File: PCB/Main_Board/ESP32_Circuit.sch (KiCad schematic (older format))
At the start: 26 parts, among them Q1 MBT3904DW1, SW2 EN, SW3 BOOT, U3 ESP32-WROOM-32, U4 FT231XS

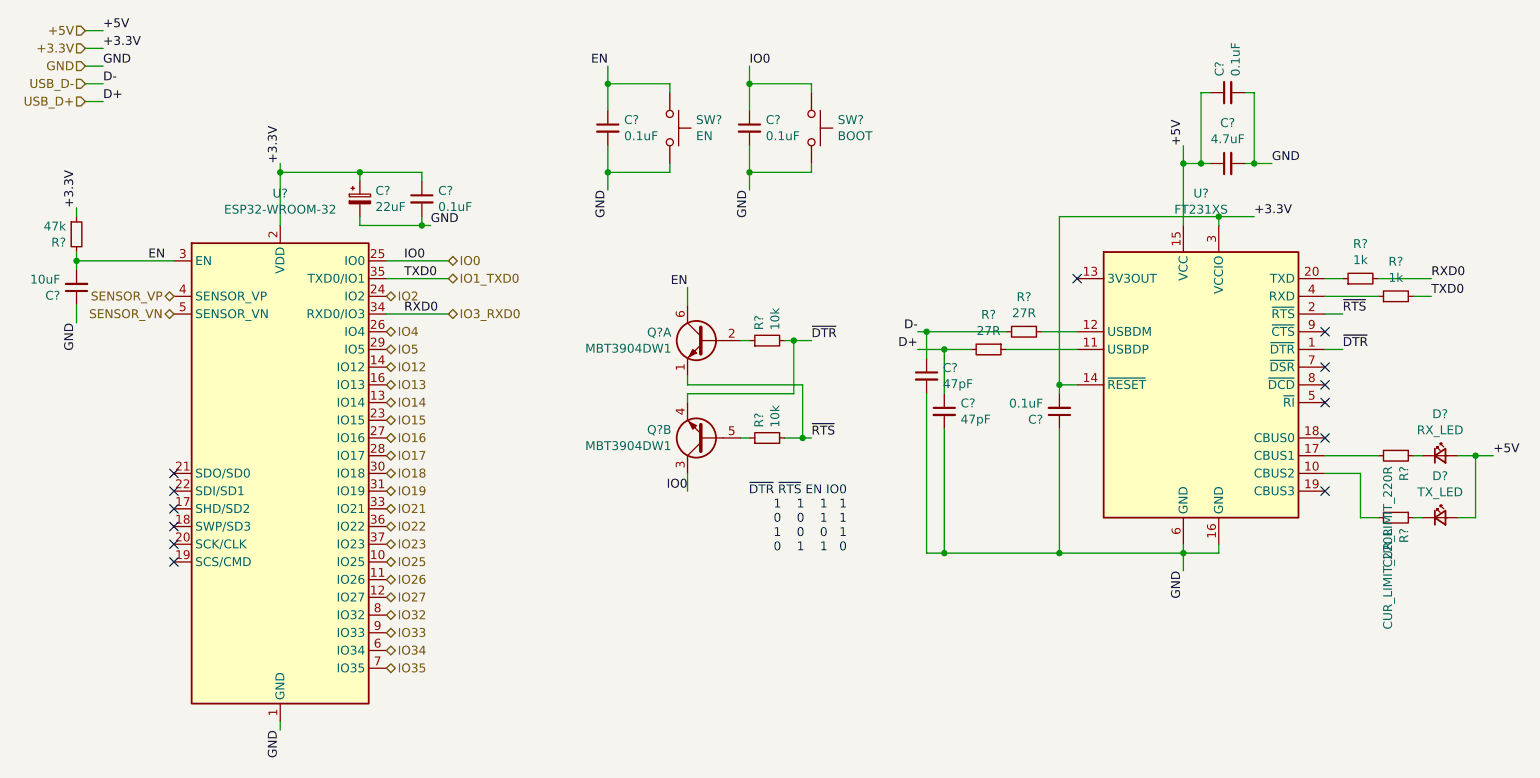
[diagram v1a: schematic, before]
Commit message: Annotate resistors
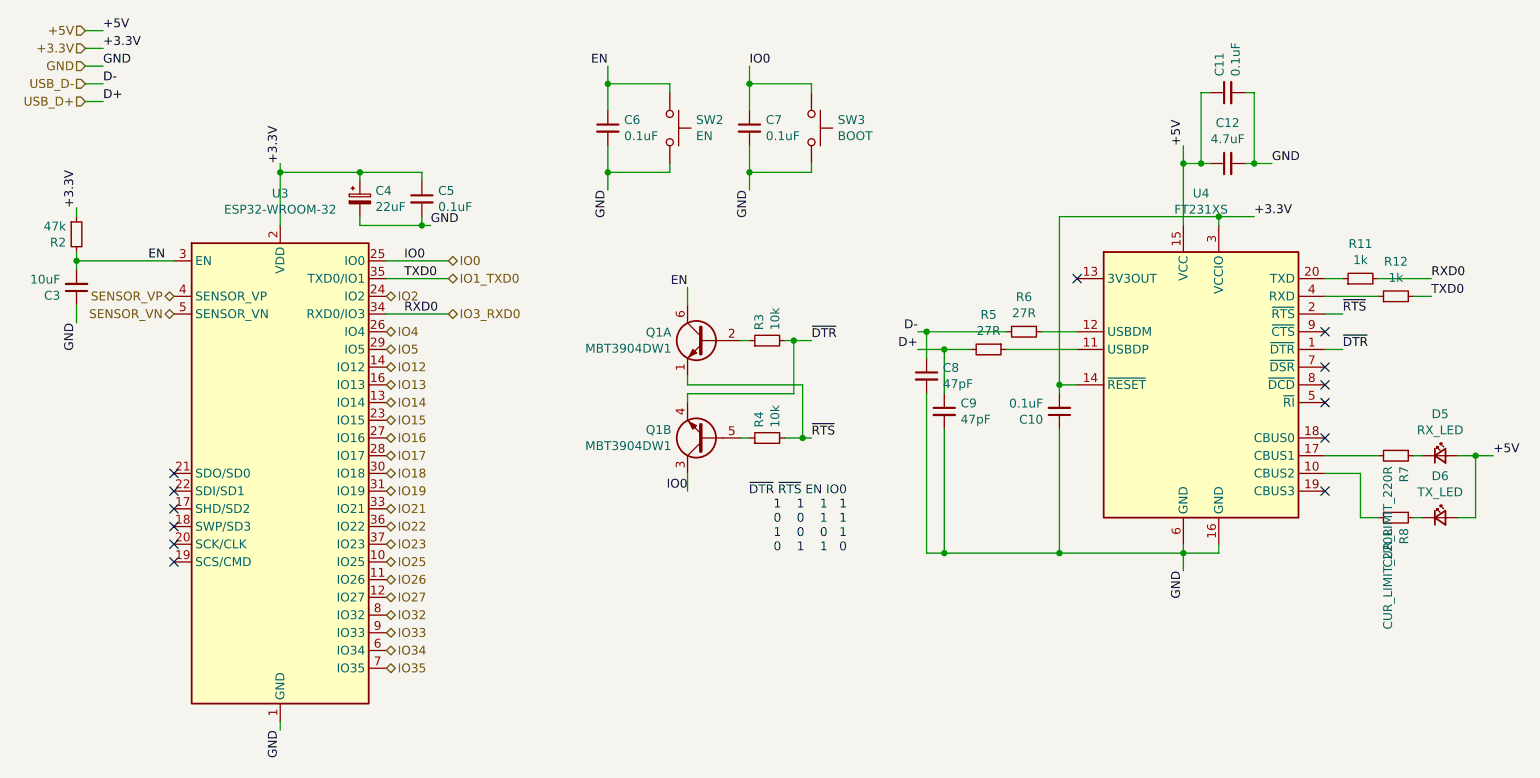
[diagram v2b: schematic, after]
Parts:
- gave numbers to parts that had none: 2
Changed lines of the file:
@@
 $Descr A4 11693 8268
 encoding utf-8
-Sheet 2 2
+Sheet 4 4
 Title "ESP32 Programming Circuit"
 Date "2020-09-10"
@@
 AR Path="/5F889015/5F5D6074" Ref="C12"  Part="1"
 AR Path="/5F80B999/5F5D6074" Ref="C?"  Part="1"
-F 0 "C?" V 8679 2400 50  0000 C CNN
+F 0 "C12" V 8679 2400 50  0000 C CNN
 F 1 "4.7uF" V 8588 2400 50  0000 C CNN
 F 2 "Capacitor_SMD:C_0603_1608Metric_Pad1.05x0.95mm_HandSolder" H 8450 2400 50  0001 C CNN
@@
 AR Path="/5F889015/5F5D607A" Ref="C11"  Part="1"
 AR Path="/5F80B999/5F5D607A" Ref="C?"  Part="1"
-F 0 "C?" H 8542 2046 50  0000 L CNN
+F 0 "C11" H 8542 2046 50  0000 L CNN
 F 1 "0.1uF" H 8542 1955 50  0000 L CNN
 F 2 "Capacitor_SMD:C_0603_1608Metric_Pad1.05x0.95mm_HandSolder" H 8450 2000 50  0001 C CNN
@@
 AR Path="/5F889015/5F5D6093" Ref="C10"  Part="1"
 AR Path="/5F80B999/5F5D6093" Ref="C?"  Part="1"
-F 0 "C?" H 7592 3846 50  0000 L CNN
+F 0 "C10" H 7592 3846 50  0000 L CNN
 F 1 "0.1uF" H 7592 3755 50  0000 L CNN
 F 2 "Capacitor_SMD:C_0603_1608Metric_Pad1.05x0.95mm_HandSolder" H 7500 3800 50  0001 C CNN
@@
 AR Path="/5F889015/5F5D60AB" Ref="C8"  Part="1"
 AR Path="/5F80B999/5F5D60AB" Ref="C?"  Part="1"
-F 0 "C?" H 6842 3646 50  0000 L CNN
+F 0 "C8" H 6842 3646 50  0000 L CNN
 F 1 "47pF" H 6842 3555 50  0000 L CNN
 F 2 "Capacitor_SMD:C_0603_1608Metric_Pad1.05x0.95mm_HandSolder" H 6750 3600 50  0001 C CNN
@@
 AR Path="/5F889015/5F5D60B1" Ref="C9"  Part="1"
 AR Path="/5F80B999/5F5D60B1" Ref="C?"  Part="1"
-F 0 "C?" H 6942 3846 50  0000 L CNN
+F 0 "C9" H 6942 3846 50  0000 L CNN
 F 1 "47pF" H 6942 3755 50  0000 L CNN
 F 2 "Capacitor_SMD:C_0603_1608Metric_Pad1.05x0.95mm_HandSolder" H 6850 3800 50  0001 C CNN
@@
 AR Path="/5F889015/5F5D60CE" Ref="U4"  Part="1"
 AR Path="/5F80B999/5F5D60CE" Ref="U?"  Part="1"
-F 0 "U?" H 8300 4731 50  0000 C CNN
+F 0 "U4" H 8300 4731 50  0000 C CNN
 F 1 "FT231XS" H 8300 4640 50  0000 C CNN
 F 2 "Package_SO:SSOP-20_3.9x8.7mm_P0.635mm" H 9300 2850 50  0001 C CNN
@@
 AR Path="/5F889015/5F5D60D4" Ref="D6"  Part="1"
 AR Path="/5F80B999/5F5D60D4" Ref="D?"  Part="1"
-F 0 "D?" H 9650 4635 50  0000 C CNN
+F 0 "D6" H 9650 4635 50  0000 C CNN
 F 1 "TX_LED" H 9650 4544 50  0000 C CNN
 F 2 "LED_SMD:LED_0603_1608Metric_Pad1.05x0.95mm_HandSolder" V 9650 4400 50  0001 C CNN
@@
 AR Path="/5F889015/5F5D60DB" Ref="R8"  Part="1"
 AR Path="/5F80B999/5F5D60DB" Ref="R?"  Part="1"
-F 0 "R?" H 9459 4446 50  0000 L CNN
+F 0 "R8" H 9459 4446 50  0000 L CNN
 F 1 "CUR_LIMIT_220R" H 9459 4355 50  0000 L CNN
 F 2 "Resistor_SMD:R_0603_1608Metric_Pad1.05x0.95mm_HandSolder" H 9400 4400 50  0001 C CNN
@@
 AR Path="/5F889015/5F5D60E1" Ref="D5"  Part="1"
 AR Path="/5F80B999/5F5D60E1" Ref="D?"  Part="1"
-F 0 "D?" H 9650 4285 50  0000 C CNN
+F 0 "D5" H 9650 4285 50  0000 C CNN
 F 1 "RX_LED" H 9650 4194 50  0000 C CNN
 F 2 "LED_SMD:LED_0603_1608Metric_Pad1.05x0.95mm_HandSolder" V 9650 4050 50  0001 C CNN
@@
 AR Path="/5F889015/5F5D60E8" Ref="R7"  Part="1"
 AR Path="/5F80B999/5F5D60E8" Ref="R?"  Part="1"
-F 0 "R?" H 9459 4096 50  0000 L CNN
+F 0 "R7" H 9459 4096 50  0000 L CNN
 F 1 "CUR_LIMIT_220R" H 9459 4005 50  0000 L CNN
 F 2 "Resistor_SMD:R_0603_1608Metric_Pad1.05x0.95mm_HandSolder" H 9400 4050 50  0001 C CNN
@@
 AR Path="/5F889015/5F5F2511" Ref="U3"  Part="1"
 AR Path="/5F80B999/5F5F2511" Ref="U?"  Part="1"
-F 0 "U?" H 3100 5731 50  0000 C CNN
+F 0 "U3" H 3100 5731 50  0000 C CNN
 F 1 "ESP32-WROOM-32" H 3100 5640 50  0000 C CNN
 F 2 "RF_Module:ESP32-WROOM-32" H 3100 2650 50  0001 C CNN
@@
 AR Path="/5F889015/5F5F251D" Ref="C4"  Part="1"
 AR Path="/5F80B999/5F5F251D" Ref="C?"  Part="1"
-F 0 "C?" H 3638 2646 50  0000 L CNN
+F 0 "C4" H 3638 2646 50  0000 L CNN
 F 1 "22uF" H 3638 2555 50  0000 L CNN
 F 2 "Capacitor_SMD:C_0603_1608Metric_Pad1.05x0.95mm_HandSolder" H 3550 2600 50  0001 C CNN
@@
 AR Path="/5F889015/5F5F2523" Ref="C5"  Part="1"
 AR Path="/5F80B999/5F5F2523" Ref="C?"  Part="1"
-F 0 "C?" H 3992 2646 50  0000 L CNN
+F 0 "C5" H 3992 2646 50  0000 L CNN
 F 1 "0.1uF" H 3992 2555 50  0000 L CNN
 F 2 "Capacitor_SMD:C_0603_1608Metric_Pad1.05x0.95mm_HandSolder" H 3900 2600 50  0001 C CNN
@@
 AR Path="/5F889015/5F5F2548" Ref="C3"  Part="1"
 AR Path="/5F80B999/5F5F2548" Ref="C?"  Part="1"
-F 0 "C?" H 2042 3146 50  0000 L CNN
+F 0 "C3" H 2042 3146 50  0000 L CNN
 F 1 "10uF" H 2042 3055 50  0000 L CNN
 F 2 "Capacitor_SMD:C_0603_1608Metric_Pad1.05x0.95mm_HandSolder" H 1950 3100 50  0001 C CNN
@@
 AR Path="/5F889015/5F5F254F" Ref="C6"  Part="1"
 AR Path="/5F80B999/5F5F254F" Ref="C?"  Part="1"
-F 0 "C?" H 5042 2246 50  0000 L CNN
+F 0 "C6" H 5042 2246 50  0000 L CNN
 F 1 "0.1uF" H 5042 2155 50  0000 L CNN
 F 2 "Capacitor_SMD:C_0603_1608Metric_Pad1.05x0.95mm_HandSolder" H 4950 2200 50  0001 C CNN
@@
 AR Path="/5F889015/5F5F2568" Ref="SW2"  Part="1"
 AR Path="/5F80B999/5F5F2568" Ref="SW?"  Part="1"
-F 0 "SW?" V 5254 2348 50  0000 L CNN
+F 0 "SW2" V 5254 2348 50  0000 L CNN
 F 1 "EN" V 5345 2348 50  0000 L CNN
 F 2 "SamacSys:SKTHAHE010" H 5300 2400 50  0001 C CNN
@@
 AR Path="/5F889015/5F5F2577" Ref="C7"  Part="1"
 AR Path="/5F80B999/5F5F2577" Ref="C?"  Part="1"
-F 0 "C?" H 5842 2246 50  0000 L CNN
+F 0 "C7" H 5842 2246 50  0000 L CNN
 F 1 "0.1uF" H 5842 2155 50  0000 L CNN
 F 2 "Capacitor_SMD:C_0603_1608Metric_Pad1.05x0.95mm_HandSolder" H 5750 2200 50  0001 C CNN
@@
 AR Path="/5F889015/5F5F258F" Ref="SW3"  Part="1"
 AR Path="/5F80B999/5F5F258F" Ref="SW?"  Part="1"
-F 0 "SW?" V 6054 2348 50  0000 L CNN
+F 0 "SW3" V 6054 2348 50  0000 L CNN
 F 1 "BOOT" V 6145 2348 50  0000 L CNN
 F 2 "SamacSys:SKTHAHE010" H 6100 2400 50  0001 C CNN
@@
 AR Path="/5F889015/5F5F2599" Ref="Q1"  Part="1"
 AR Path="/5F80B999/5F5F2599" Ref="Q?"  Part="1"
-F 0 "Q?" H 5691 3446 50  0000 L CNN
+F 0 "Q1" H 5691 3446 50  0000 L CNN
 F 1 "MBT3904DW1" H 5691 3355 50  0000 L CNN
 F 2 "Package_TO_SOT_SMD:SOT-363_SC-70-6" H 5700 3500 50  0001 C CNN
@@
 AR Path="/5F889015/5F5F259F" Ref="Q1"  Part="2"
 AR Path="/5F80B999/5F5F259F" Ref="Q?"  Part="2"
-F 0 "Q?" H 5691 3904 50  0000 L CNN
+F 0 "Q1" H 5691 3904 50  0000 L CNN
 F 1 "MBT3904DW1" H 5691 3995 50  0000 L CNN
 F 2 "Package_TO_SOT_SMD:SOT-363_SC-70-6" H 5700 4050 50  0001 C CNN
@@
 AR Path="/5F889015/5F5F25A5" Ref="R3"  Part="1"
 AR Path="/5F80B999/5F5F25A5" Ref="R?"  Part="1"
-F 0 "R?" H 5909 3446 50  0000 L CNN
+F 0 "R3" H 5909 3446 50  0000 L CNN
 F 1 "10k" H 5909 3355 50  0000 L CNN
 F 2 "Resistor_SMD:R_0603_1608Metric_Pad1.05x0.95mm_HandSolder" H 5850 3400 50  0001 C CNN
@@
 AR Path="/5F889015/5F5F25AB" Ref="R4"  Part="1"
 AR Path="/5F80B999/5F5F25AB" Ref="R?"  Part="1"
-F 0 "R?" H 5909 3996 50  0000 L CNN
+F 0 "R4" H 5909 3996 50  0000 L CNN
 F 1 "10k" H 5909 3905 50  0000 L CNN
 F 2 "Resistor_SMD:R_0603_1608Metric_Pad1.05x0.95mm_HandSolder" H 5850 3950 50  0001 C CNN
@@
 AR Path="/5F889015/5F5F2542" Ref="R2"  Part="1"
 AR Path="/5F80B999/5F5F2542" Ref="R?"  Part="1"
-F 0 "R?" H 1891 2754 50  0000 R CNN
+F 0 "R2" H 1891 2754 50  0000 R CNN
 F 1 "47k" H 1891 2845 50  0000 R CNN
 F 2 "Resistor_SMD:R_0603_1608Metric_Pad1.05x0.95mm_HandSolder" H 1950 2800 50  0001 C CNN
@@
 AR Path="/5F889015/5F5D60A4" Ref="R5"  Part="1"
 AR Path="/5F80B999/5F5D60A4" Ref="R?"  Part="1"
-F 0 "R?" V 6904 3450 50  0000 C CNN
+F 0 "R5" V 6904 3450 50  0000 C CNN
 F 1 "27R" V 6995 3450 50  0000 C CNN
 F 2 "Resistor_SMD:R_0603_1608Metric_Pad1.05x0.95mm_HandSolder" H 7100 3450 50  0001 C CNN
@@
 AR Path="/5F889015/5F5D609E" Ref="R6"  Part="1"
 AR Path="/5F80B999/5F5D609E" Ref="R?"  Part="1"
-F 0 "R?" V 7104 3350 50  0000 C CNN
+F 0 "R6" V 7104 3350 50  0000 C CNN
 F 1 "27R" V 7195 3350 50  0000 C CNN
 F 2 "Resistor_SMD:R_0603_1608Metric_Pad1.05x0.95mm_HandSolder" H 7300 3350 50  0001 C CNN
@@
 Connection ~ 8400 2700
 $Comp
-L Device:R_Small R?
+L Device:R_Small R11
 U 1 1 5F79186D
 P 9200 3050
-F 0 "R?" V 9396 3050 50  0000 C CNN
+F 0 "R11" V 9396 3050 50  0000 C CNN
 F 1 "1k" V 9305 3050 50  0000 C CNN
 F 2 "" H 9200 3050 50  0001 C CNN
@@
 $EndComp
 $Comp
-L Device:R_Small R?
+L Device:R_Small R12
 U 1 1 5F7A23BF
 P 9400 3150
-F 0 "R?" V 9596 3150 50  0000 C CNN
+F 0 "R12" V 9596 3150 50  0000 C CNN
 F 1 "1k" V 9505 3150 50  0000 C CNN
 F 2 "" H 9400 3150 50  0001 C CNN

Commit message: Update KiCAD to 5.1.7 and change a couple of footprints
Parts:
- Q1: footprint Package_TO_SOT_SMD:SOT-363_SC-70-6 -> Package_TO_SOT_SMD:SOT-363_SC-70-6_Handsoldering
- R11, R12: footprint (none) -> Resistor_SMD:R_0603_1608Metric_Pad0.98x0.95mm_HandSolder
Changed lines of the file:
@@
 F 0 "Q1" H 5691 3446 50  0000 L CNN
 F 1 "MBT3904DW1" H 5691 3355 50  0000 L CNN
-F 2 "Package_TO_SOT_SMD:SOT-363_SC-70-6" H 5700 3500 50  0001 C CNN
+F 2 "Package_TO_SOT_SMD:SOT-363_SC-70-6_Handsoldering" H 5700 3500 50  0001 C CNN
 F 3 "http://www.onsemi.com/pub_link/Collateral/MBT3904DW1T1-D.PDF" H 5500 3400 50  0001 C CNN
 	1    5500 3400
@@
 F 0 "Q1" H 5691 3904 50  0000 L CNN
 F 1 "MBT3904DW1" H 5691 3995 50  0000 L CNN
-F 2 "Package_TO_SOT_SMD:SOT-363_SC-70-6" H 5700 4050 50  0001 C CNN
+F 2 "Package_TO_SOT_SMD:SOT-363_SC-70-6_Handsoldering" H 5700 4050 50  0001 C CNN
 F 3 "http://www.onsemi.com/pub_link/Collateral/MBT3904DW1T1-D.PDF" H 5500 3950 50  0001 C CNN
 	2    5500 3950
@@
 F 0 "R11" V 9396 3050 50  0000 C CNN
 F 1 "1k" V 9305 3050 50  0000 C CNN
-F 2 "" H 9200 3050 50  0001 C CNN
+F 2 "Resistor_SMD:R_0603_1608Metric_Pad0.98x0.95mm_HandSolder" H 9200 3050 50  0001 C CNN
 F 3 "~" H 9200 3050 50  0001 C CNN
 	1    9200 3050
@@
 F 0 "R12" V 9596 3150 50  0000 C CNN
 F 1 "1k" V 9505 3150 50  0000 C CNN
-F 2 "" H 9400 3150 50  0001 C CNN
+F 2 "Resistor_SMD:R_0603_1608Metric_Pad0.98x0.95mm_HandSolder" H 9400 3150 50  0001 C CNN
 F 3 "~" H 9400 3150 50  0001 C CNN
 	1    9400 3150
